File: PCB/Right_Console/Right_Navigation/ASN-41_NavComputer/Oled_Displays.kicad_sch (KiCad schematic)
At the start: 17 parts, among them U10 ER_OLEDM0.91_1x-I2C, U11 ER_OLEDM0.91_1x-I2C, U4 TCA9548APWR, U5 ER_OLEDM0.91_1x-I2C, U6 ER_OLEDM0.91_1x-I2C, U7 ER_OLEDM0.91_1x-I2C, U8 ER_OLEDM0.91_1x-I2C, U9 ER_OLEDM0.91_1x-I2C

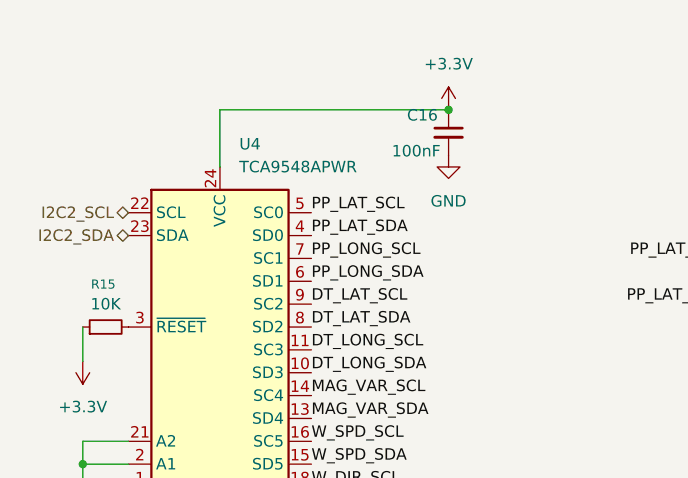
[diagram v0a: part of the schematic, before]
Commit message: feat(pcb): label LCSC/tolerance/voltage across fleet boards (Right_Nav + PDU + base) (#235)
Populates **LCSC part number + tolerance + voltage** fields across all
six fleet boards, so each schematic drives an orderable BOM.

## Boards labeled (ERC 0/0 on all)
- **Right_Nav:** ASN-41, ARC-51A, APN-153
- **Power:** PDU
- **Base:** Gateway_Bridge, PanelGroup_Base

## What it does
- LCSC + tolerance + voltage on every assembled part, corrected to the
selected part (100nF 50V, resistors 1%, AMS1117 C6186→C347222, 10µF
split 25V/35V by +12V rail).
- Off-board panel controls (encoders, rotary switches, OLED, pot,
stepper, MEM button) left blank — connector-coupled, no assembly LCSC.
- Pin headers hand-soldered; RP2040-Zero left blank (module, sourced
separately).

## Design corrections captured here
- **PDU 1k series/anti-alias → 1%** (C110774 0.1% → C844939): precision
belongs only on the divider ratio resistors (33k/13k/10k); the series 1k
sit into high-Z ADC pins where 1% is identical. Drops the precision part
from the board.
- **DESIGN-NOTES:** records the 1k downgrade + the order-time shunt
upgrade (C346481 ±100ppm → C500740 ±25ppm, drop-in 2512).

## Not in this PR (follow-ups)
- Fleet component **standardization** (10µF-bulk→electrolytic,
consolidate to single 35V value, IPN convention) — separate pass.
- InvenTree backfill of the new SKUs.
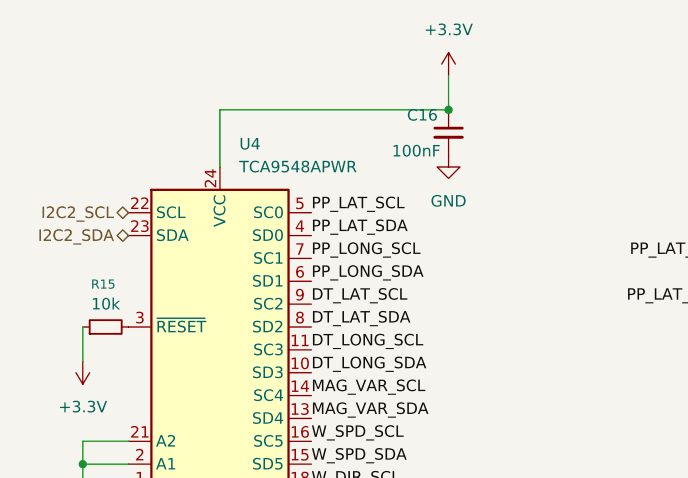
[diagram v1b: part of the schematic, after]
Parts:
- C16, C17, C18, C19, C20, C21, C22, C23: LCSC (none) -> C1711; Rating 16V -> 50V
- R15: value 10K -> 10k; LCSC (none) -> C844937; Tolerance 5% -> 1%
